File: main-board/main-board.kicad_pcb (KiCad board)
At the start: 4 copper layers, 241.7 x 56.7 mm, 141 parts, among them J1 NCJ6FA-H-0, J10 SDS-50J, J11 Conn_02x14_Odd_Even, J12 Conn_02x02_Odd_Even, J13 Barrel_Jack_MountingPin, J14 Micro_SD_Card_Det2, J2 NCJ6FA-H-0, J3 Conn_02x10_Odd_Even, J4 NCJ6FA-H-0, J6 NCJ6FA-H-0, J7 SDS-50J, J8 Conn_02x03, J9 SDS-50J, Q1 MMBT3904, Q2 MMBT3906, Q3 MMBT3906, Q4 MMBT3904, Q5 DMP3056L-13, SW1 Power, U1 THAT1646, U10 TPS54302, U2 THAT1646, U3 OPA1656ID, U4 THAT1246, U5 THAT1246, U6 OPA1656ID, U7 LM2903, U8 H11L1, U9 Daisy_Seed

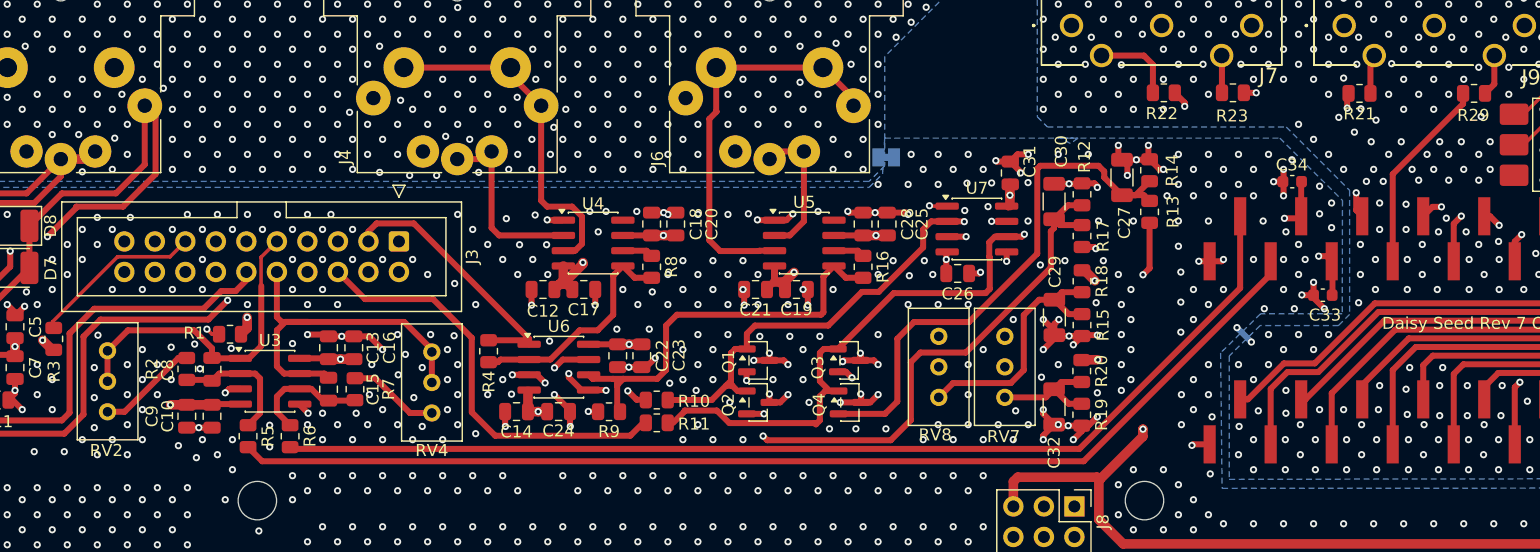
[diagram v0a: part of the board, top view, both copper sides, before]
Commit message: Tackle pre expermintal work (#28)
**Pre-experimental fixes — #18 #19 #20 #21**

Four correctness fixes on the input clamp circuit before the next experimental round:

- **Clamp transistor footprint** (#18): Switched Q_clamp from TO-92 (2N3906) to SOT-23 (PZT3906) — updates datasheet, description, sim pin mapping (B/E/C), and footprint filter in the PCB.
- **Threshold trimmer value** (#19): Raised RV_threshold from 10k → 100k so the wiper no longer drags down the clamp reference positive rail.
- **Sense line placement notes** (#20): Added schematic annotations directing R8 and R16 close to U6b to keep the sense lines short; corrected junction positions in the output topology section.
- **RV8/RV7 swap and labels** (#21): Swapped the two trimmers and added labels so they place cleanly on the PCB.

No functional changes to signal path topology — all changes are component selection, value correction, placement guidance, or layout clarity.

* swap and label rv8/7 so they lay out clearly - fixes #21
* fix sense error for output topology - fixes #20
* make threshold trimmer 100k so it doesn't drag down the clamp ref +ve rail - fixes #19
* fix footprint on the clamp transistors - fixes #18
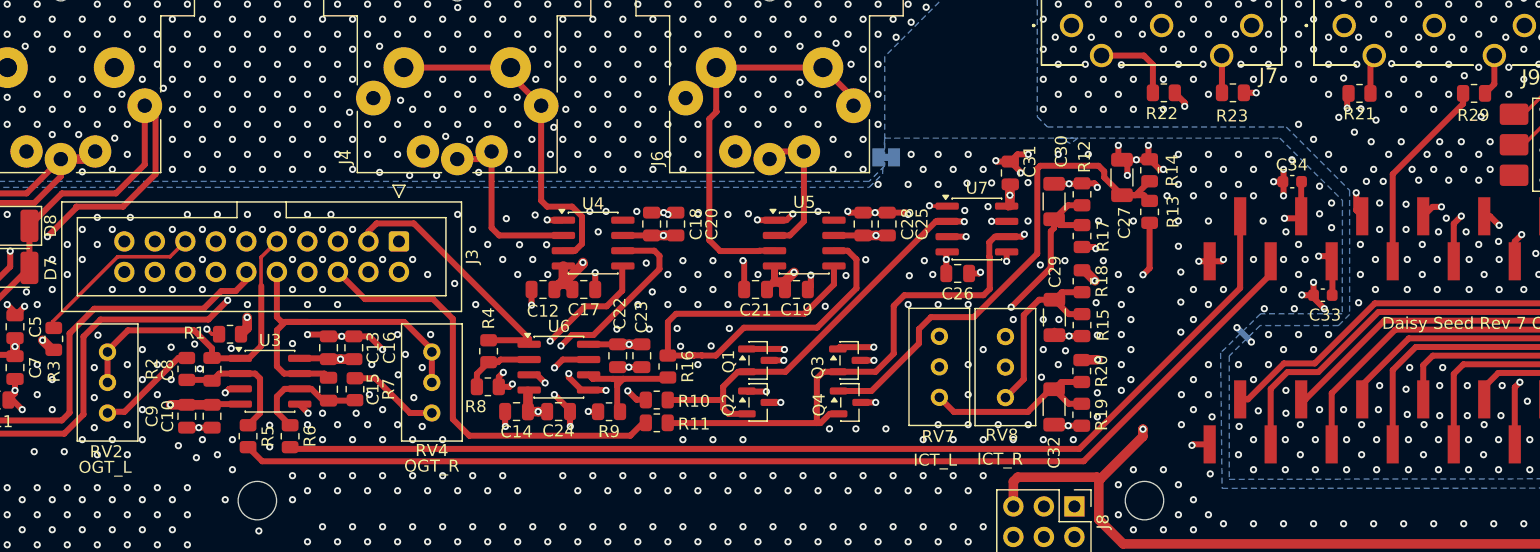
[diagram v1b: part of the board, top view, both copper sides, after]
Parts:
- RV7, RV8: value 10k -> 100k
- moved R16 18.2 mm to (114.3, 66.3)
- moved R8 16.9 mm to (99.3, 68.0), turned to 180 degrees
- moved RV8 5.55 mm to (142.4, 68.9)
- moved RV7 5.45 mm to (136.9, 68.9)
- moved RV2 0.10 mm to (67.7, 65.1)
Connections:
- Q1 pad 1: AUDIO_IN_L -> -VCLAMP_L
- Q1 pad 2: -VCLAMP_L -> AUDIO_IN_L
- Q2 pad 1: AUDIO_IN_L -> +VCLAMP_L
- Q2 pad 2: +VCLAMP_L -> AUDIO_IN_L
- Q3 pad 1: AUDIO_IN_R -> +VCLAMP_R
- Q3 pad 2: +VCLAMP_R -> AUDIO_IN_R
- Q4 pad 1: AUDIO_IN_R -> -VCLAMP_R
- Q4 pad 2: -VCLAMP_R -> AUDIO_IN_R
- R16 pad 1: Net-(R16-Pad1) -> Net-(U5A-S)
- R16 pad 2: Net-(U5A-S) -> Net-(U6B--)
- R4 pad 1: Net-(U4A-S) -> Net-(U6A--)
- R8 pad 1: Net-(R8-Pad1) -> Net-(U4A-S)
- R8 pad 2: Net-(U4A-S) -> Net-(U6A--)
- R9 pad 1: Net-(U5A-S) -> Net-(U6B--)
- U4 pad 6: Net-(R8-Pad1) -> Net-(U4A-S)
- U5 pad 6: Net-(R16-Pad1) -> Net-(U5A-S)
- U6 pad 2: Net-(U4A-S) -> Net-(U6A--)
- U6 pad 6: Net-(U5A-S) -> Net-(U6B--)
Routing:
- net GND: track 240.2 -> 216.8 mm, vias 1779 -> 1736
- net Net-(U4A-S): track 19.2 -> 37.9 mm, vias 0 -> 4
- net Net-(U6B--): track 0.00 -> 10.3 mm
- net -VCLAMP_L: track 48.2 -> 38.5 mm
- net Net-(U5A-S): track 34.7 -> 42.1 mm
- net Net-(U6A--): track 0.00 -> 5.92 mm
- net -VCLAMP_R: track 45.9 -> 42.8 mm
- net Net-(R16-Pad1): track 2.60 -> 0.00 mm
- net Net-(R8-Pad1): track 2.58 -> 0.00 mm
- net /Audio Input/IN_THRESH_L: track 17.5 -> 15.0 mm
- net +VCLAMP_R: track 30.3 -> 31.7 mm
- net AUDIO_IN_L: track 73.2 -> 71.9 mm
- net IN_WIPER_R: track 35.1 -> 36.4 mm
- net /Audio Input/IN_THRESH_R: track 11.9 -> 10.7 mm
- net +VCLAMP_L: track 31.8 -> 32.4 mm
